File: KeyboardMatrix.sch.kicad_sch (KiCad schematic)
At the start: 72 parts, among them SW1 SW_Push_45deg, SW10 SW_Push_45deg, SW11 SW_Push_45deg, SW12 SW_Push_45deg, SW13 SW_Push_45deg, SW14 SW_Push_45deg, SW15 SW_Push_45deg, SW16 SW_Push_45deg, SW17 SW_Push_45deg, SW18 SW_Push_45deg, SW19 SW_Push_45deg, SW2 SW_Push_45deg, SW20 SW_Push_45deg, SW21 SW_Push_45deg, SW22 SW_Push_45deg, SW23 SW_Push_45deg, SW24 SW_Push_45deg, SW25 SW_Push_45deg, SW26 SW_Push_45deg, SW27 SW_Push_45deg, SW28 SW_Push_45deg, SW29 SW_Push_45deg, SW3 SW_Push_45deg, SW30 SW_Push_45deg, SW31 SW_Push_45deg, SW32 SW_Push_45deg, SW33 SW_Push_45deg, SW34 SW_Push_45deg, SW35 SW_Push_45deg, SW37 SW_Push_45deg, SW4 SW_Push_45deg, SW5 SW_Push_45deg, SW6 SW_Push_45deg, SW7 SW_Push_45deg, SW8 SW_Push_45deg, SW9 SW_Push_45deg

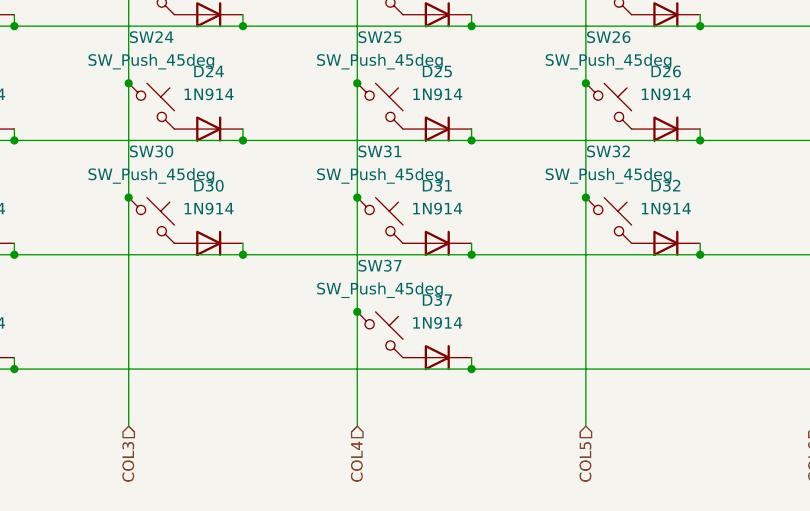
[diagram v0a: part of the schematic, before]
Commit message: Created the PCB layout
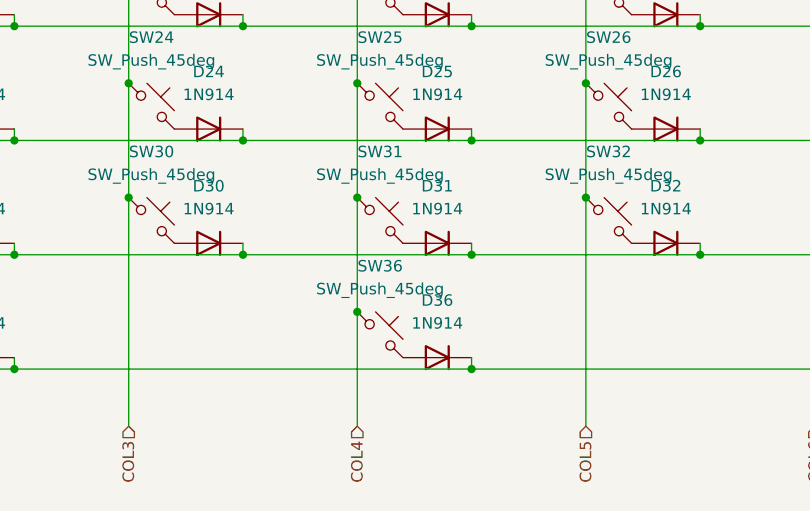
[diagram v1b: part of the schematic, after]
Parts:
- SW1, SW10, SW11, SW12, SW13, SW14, SW15, SW16, SW17, SW18, SW19, SW2, SW20, SW21, SW22, SW23, SW24, SW25, SW26, SW27, SW28, SW29, SW3, SW30, SW31, SW32, SW33, SW34, SW35, SW4, SW5, SW6, SW7, SW8, SW9: footprint (none) -> ScottoKeebs_MX:MX_PCB_1.00u
- SW36: renamed from SW37; footprint (none) -> ScottoKeebs_MX:MX_PCB_1.00u
- renumbered D37 to D36
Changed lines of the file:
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@@
 			)
 		)
-		(property "Footprint" ""
+		(property "Footprint" "ScottoKeebs_MX:MX_PCB_1.00u"
 			(at 91.44 40.64 0)
 			(hide yes)
@@
 			)
 		)
-		(property "Footprint" ""
+		(property "Footprint" "ScottoKeebs_MX:MX_PCB_1.00u"
 			(at 193.04 27.94 0)
 			(hide yes)
@@
 			)
 		)
-		(property "Footprint" ""
+		(property "Footprint" "ScottoKeebs_MX:MX_PCB_1.00u"
 			(at 116.84 40.64 0)
 			(hide yes)
@@
 			)
 		)
-		(property "Footprint" ""
+		(property "Footprint" "ScottoKeebs_MX:MX_PCB_1.00u"
 			(at 40.64 40.64 0)
 			(hide yes)
@@
 			)
 		)
-		(property "Footprint" ""
+		(property "Footprint" "ScottoKeebs_MX:MX_PCB_1.00u"
 			(at 116.84 53.34 0)
 			(hide yes)
@@
 			)
 		)
-		(property "Footprint" ""
+		(property "Footprint" "ScottoKeebs_MX:MX_PCB_1.00u"
 			(at 66.04 27.94 0)
 			(hide yes)
@@
 			)
 		)
-		(property "Footprint" ""
+		(property "Footprint" "ScottoKeebs_MX:MX_PCB_1.00u"
 			(at 116.84 78.74 0)
 			(hide yes)
@@
 			)
 		)
-		(property "Footprint" ""
+		(property "Footprint" "ScottoKeebs_MX:MX_PCB_1.00u"
 			(at 91.44 91.44 0)
 			(hide yes)
@@
 			)
 		)
-		(property "Footprint" ""
+		(property "Footprint" "ScottoKeebs_MX:MX_PCB_1.00u"
 			(at 142.24 53.34 0)
 			(hide yes)
@@
 			)
 		)
-		(property "Footprint" ""
+		(property "Footprint" "ScottoKeebs_MX:MX_PCB_1.00u"
 			(at 91.44 53.34 0)
 			(hide yes)
@@
 			)
 		)
-		(property "Footprint" ""
+		(property "Footprint" "ScottoKeebs_MX:MX_PCB_1.00u"
 			(at 66.04 40.64 0)
 			(hide yes)
@@
 			)
 		)
-		(property "Footprint" ""
+		(property "Footprint" "ScottoKeebs_MX:MX_PCB_1.00u"
 			(at 142.24 78.74 0)
 			(hide yes)
@@
 			)
 		)
-		(property "Footprint" ""
+		(property "Footprint" "ScottoKeebs_MX:MX_PCB_1.00u"
 			(at 40.64 66.04 0)
 			(hide yes)
@@
 			)
 		)
-		(property "Footprint" ""
+		(property "Footprint" "ScottoKeebs_MX:MX_PCB_1.00u"
 			(at 40.64 91.44 0)
 			(hide yes)
@@
 			)
 		)
-		(property "Footprint" ""
+		(property "Footprint" "ScottoKeebs_MX:MX_PCB_1.00u"
 			(at 91.44 78.74 0)
 			(hide yes)
@@
 		(dnp no)
 		(fields_autoplaced yes)
-		(property "Reference" "D37"
+		(property "Reference" "D36"
 			(at 148.59 87.63 0)
 			(show_name no)
@@
 			(project "Split Keyboard"
 				(path "/2cdc3fbd-f3ff-412c-a809-7e2f4dbd156a/763d1cfc-4401-4aac-ad6b-7ea06fb08f8c"
-					(reference "D37")
+					(reference "D36")
 					(unit 1)
 				)
@@
 			)
 		)
-		(property "Footprint" ""
+		(property "Footprint" "ScottoKeebs_MX:MX_PCB_1.00u"
 			(at 142.24 27.94 0)
 			(hide yes)
@@
 			)
 		)
-		(property "Footprint" ""
+		(property "Footprint" "ScottoKeebs_MX:MX_PCB_1.00u"
 			(at 167.64 27.94 0)
 			(hide yes)
@@
 			)
 		)
-		(property "Footprint" ""
+		(property "Footprint" "ScottoKeebs_MX:MX_PCB_1.00u"
 			(at 66.04 91.44 0)
 			(hide yes)
@@
 			)
 		)
-		(property "Footprint" ""
+		(property "Footprint" "ScottoKeebs_MX:MX_PCB_1.00u"
 			(at 40.64 78.74 0)
 			(hide yes)
@@
 			)
 		)
-		(property "Footprint" ""
+		(property "Footprint" "ScottoKeebs_MX:MX_PCB_1.00u"
 			(at 91.44 66.04 0)
 			(hide yes)
@@
 			)
 		)
-		(property "Footprint" ""
+		(property "Footprint" "ScottoKeebs_MX:MX_PCB_1.00u"
 			(at 142.24 40.64 0)
 			(hide yes)
@@
 			)
 		)
-		(property "Footprint" ""
+		(property "Footprint" "ScottoKeebs_MX:MX_PCB_1.00u"
 			(at 40.64 53.34 0)
 			(hide yes)
@@
 			)
 		)
-		(property "Footprint" ""
+		(property "Footprint" "ScottoKeebs_MX:MX_PCB_1.00u"
 			(at 167.64 40.64 0)
 			(hide yes)
@@
 			)
 		)
-		(property "Footprint" ""
+		(property "Footprint" "ScottoKeebs_MX:MX_PCB_1.00u"
 			(at 142.24 66.04 0)
 			(hide yes)
@@
 			)
 		)
-		(property "Footprint" ""
+		(property "Footprint" "ScottoKeebs_MX:MX_PCB_1.00u"
 			(at 66.04 53.34 0)
 			(hide yes)
@@
 			)
 		)
-		(property "Footprint" ""
+		(property "Footprint" "ScottoKeebs_MX:MX_PCB_1.00u"
 			(at 91.44 27.94 0)
 			(hide yes)
@@
 			)
 		)
-		(property "Footprint" ""
+		(property "Footprint" "ScottoKeebs_MX:MX_PCB_1.00u"
 			(at 167.64 78.74 0)
 			(hide yes)
@@
 			)
 		)
-		(property "Footprint" ""
+		(property "Footprint" "ScottoKeebs_MX:MX_PCB_1.00u"
 			(at 116.84 66.04 0)
 			(hide yes)
@@
 			)
 		)
-		(property "Footprint" ""
+		(property "Footprint" "ScottoKeebs_MX:MX_PCB_1.00u"
 			(at 66.04 78.74 0)
 			(hide yes)
@@
 			)
 		)
-		(property "Footprint" ""
+		(property "Footprint" "ScottoKeebs_MX:MX_PCB_1.00u"
 			(at 167.64 53.34 0)
 			(hide yes)
@@
 			)
 		)
-		(property "Footprint" ""
+		(property "Footprint" "ScottoKeebs_MX:MX_PCB_1.00u"
 			(at 167.64 66.04 0)
 			(hide yes)
@@
 			)
 		)
-		(property "Footprint" ""
+		(property "Footprint" "ScottoKeebs_MX:MX_PCB_1.00u"
 			(at 66.04 66.04 0)
 			(hide yes)
@@
 			)
 		)
-		(property "Footprint" ""
+		(property "Footprint" "ScottoKeebs_MX:MX_PCB_1.00u"
 			(at 40.64 27.94 0)
 			(hide yes)
@@
 			)
 		)
-		(property "Footprint" ""
+		(property "Footprint" "ScottoKeebs_MX:MX_PCB_1.00u"
 			(at 116.84 27.94 0)
 			(hide yes)
@@
 		(dnp no)
 		(fields_autoplaced yes)
-		(property "Reference" "SW37"
+		(property "Reference" "SW36"
 			(at 142.24 83.82 0)
 			(show_name no)
@@
 			)
 		)
-		(property "Footprint" ""
+		(property "Footprint" "ScottoKeebs_MX:MX_PCB_1.00u"
 			(at 142.24 91.44 0)
 			(hide yes)
@@
 			(project "Split Keyboard"
 				(path "/2cdc3fbd-f3ff-412c-a809-7e2f4dbd156a/763d1cfc-4401-4aac-ad6b-7ea06fb08f8c"
-					(reference "SW37")
+					(reference "SW36")
 					(unit 1)
 				)
@@
 			)
 		)
-		(property "Footprint" ""
+		(property "Footprint" "ScottoKeebs_MX:MX_PCB_1.00u"
 			(at 193.04 40.64 0)
 			(hide yes)
